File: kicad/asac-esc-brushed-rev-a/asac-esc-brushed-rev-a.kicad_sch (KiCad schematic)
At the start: 21 parts, among them J1 M1, J14 Conn_01x03, J2 Battery, J3 FC Connector, Q1 AO3480C, U1 HT7533S, U2 INA180A4, U3 STM32C011F6Px

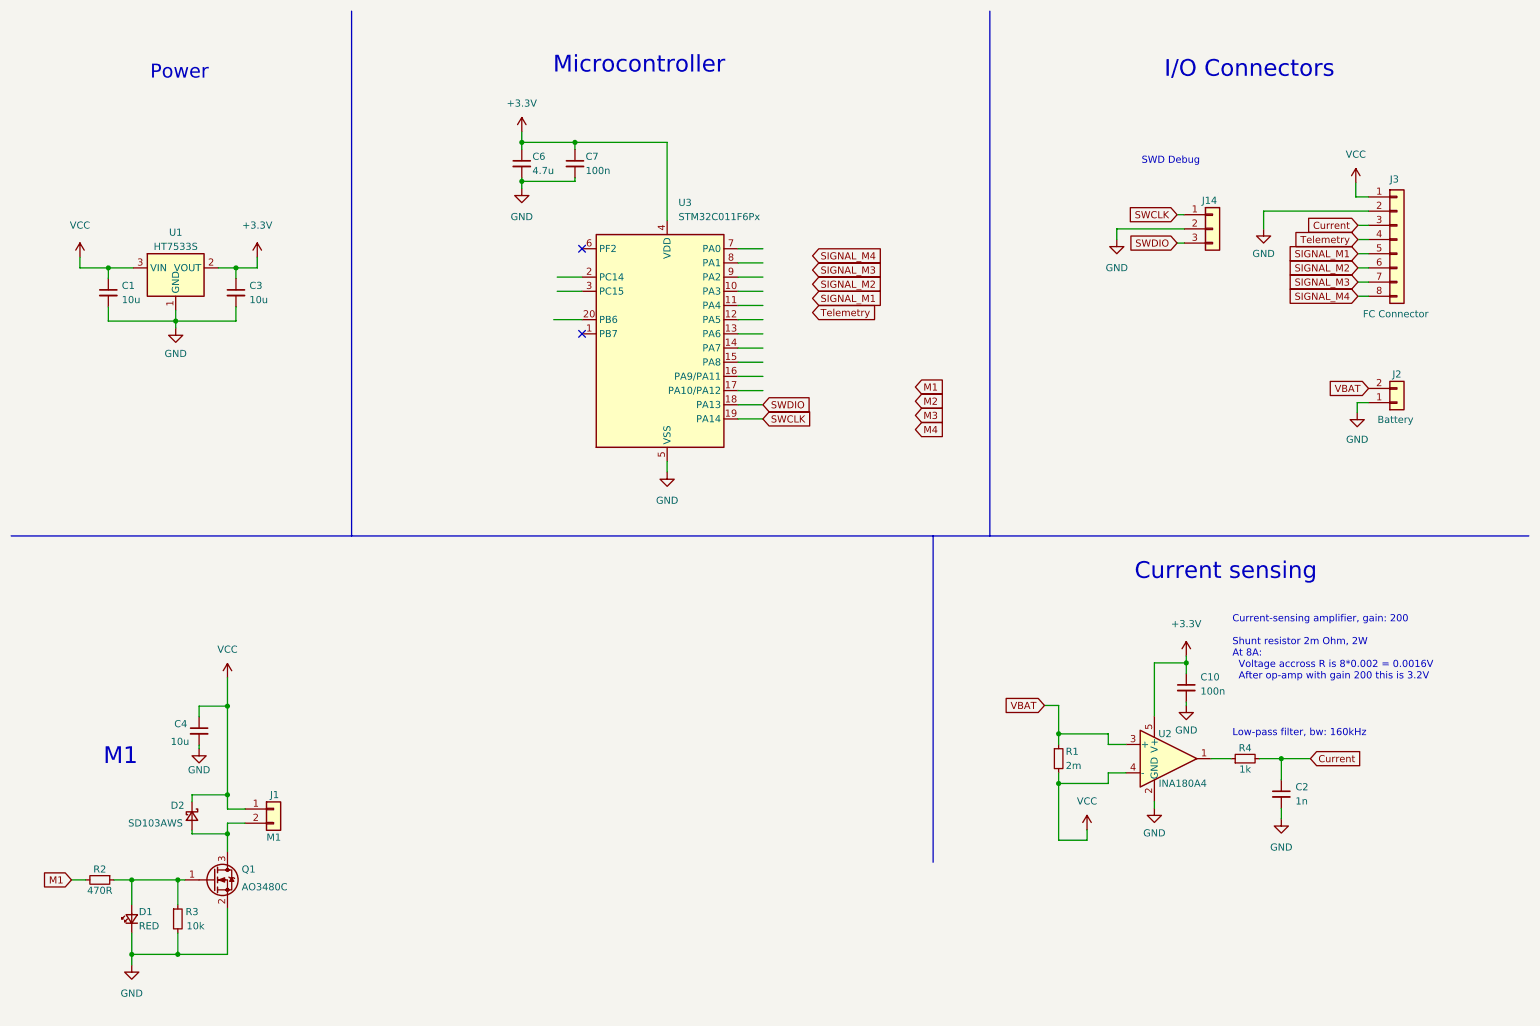
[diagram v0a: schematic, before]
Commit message: Finished rev A schematic, layout and routing
All that is left now is to add some graphics!
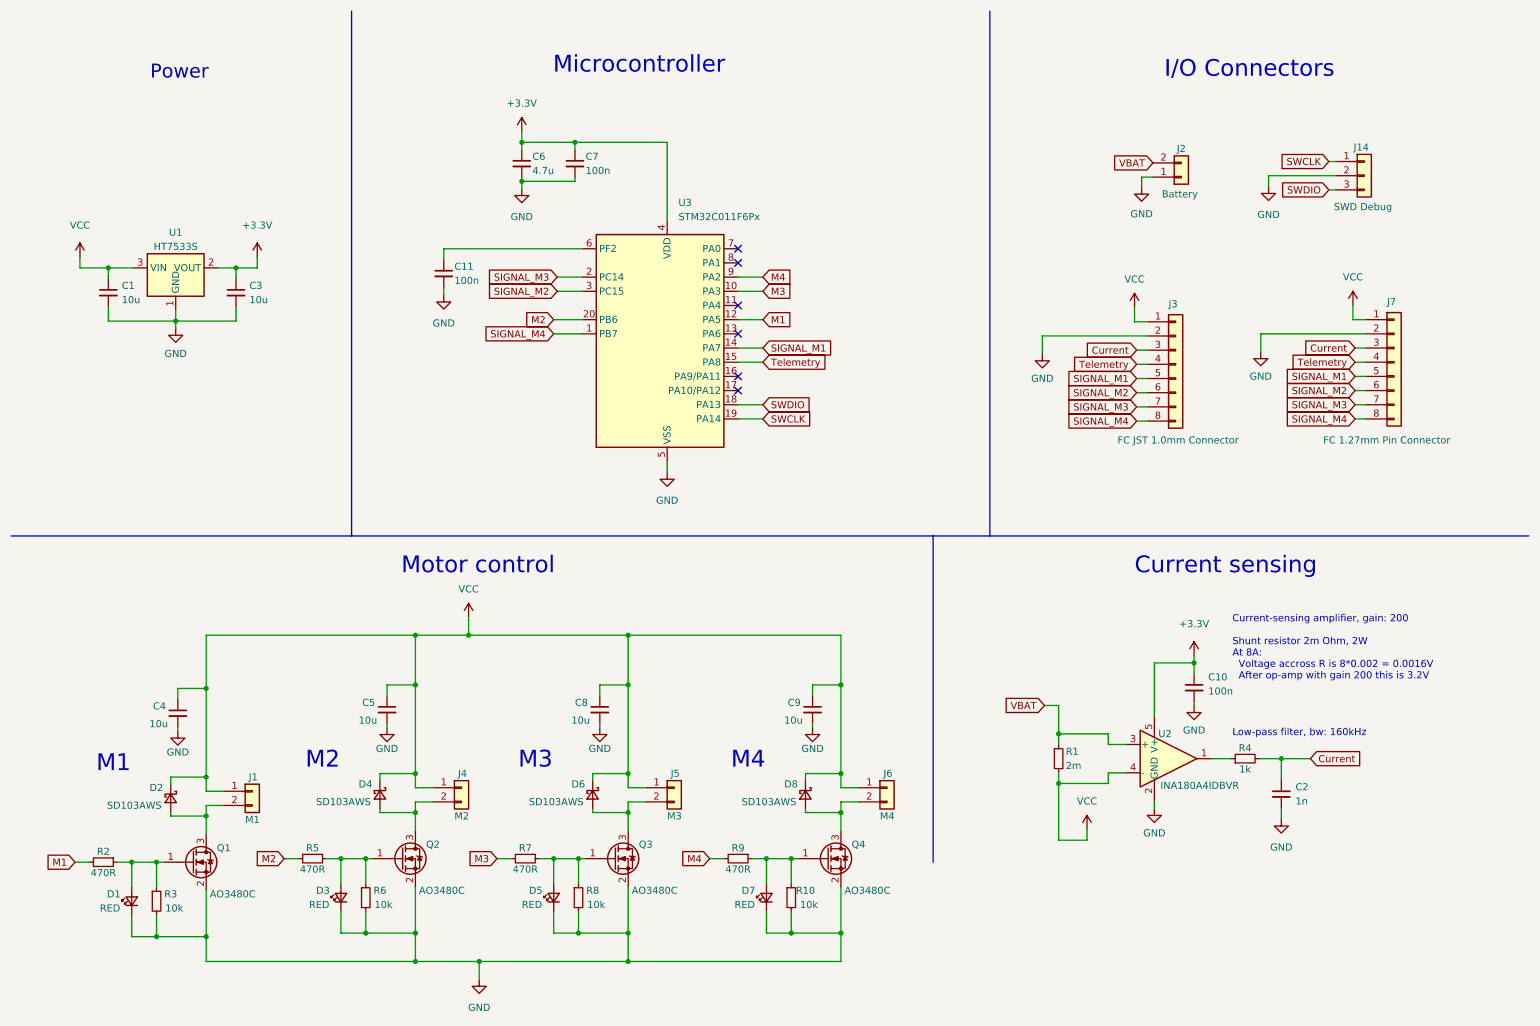
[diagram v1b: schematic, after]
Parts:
- added C11: 100n, Capacitor_SMD:C_0402_1005Metric, symbol Device:C_Small
- added C5, C8, C9: 10u, Capacitor_SMD:C_0805_2012Metric, symbol Device:C_Small
- added D3, D5, D7: RED, LED_SMD:LED_0603_1608Metric, symbol Device:LED_Small
- added D4, D6, D8: SD103AWS, Diode_SMD:D_SOD-323, symbol Device:D_Schottky_Small
- added J4: M2, Custom:Conn_01x02_VBAT_one_round, symbol Connector_Generic:Conn_01x02
- added J5: M3, Custom:Conn_01x02_VBAT_one_round, symbol Connector_Generic:Conn_01x02
- added J6: M4, Custom:Conn_01x02_VBAT_one_round, symbol Connector_Generic:Conn_01x02
- added J7: FC 1.27mm Pin Connector, Connector_PinHeader_1.27mm:PinHeader_1x08_P1.27mm_Vertical, symbol Connector_Generic:Conn_01x08
- added Q2, Q3, Q4: AO3480C, Package_TO_SOT_SMD:SOT-23, symbol Device:Q_NMOS_GSD
- added R10, R6, R8: 10k, Resistor_SMD:R_0402_1005Metric, symbol Device:R_Small
- added R5, R7, R9: 470R, Resistor_SMD:R_0402_1005Metric, symbol Device:R_Small
- J14: value Conn_01x03 -> SWD Debug
- J3: value FC Connector -> FC JST 1.0mm Connector
- U2: value INA180A4 -> INA180A4IDBVR
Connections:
- net Current: now also J7.3 (Pin_3)
- net GND: now also C11.2, C5.2, C8.2, C9.2, D3.1 (K), D5.1 (K), D7.1 (K), J7.2 (Pin_2), Q2.2 (S), Q3.2 (S), Q4.2 (S), R10.2, R6.2, R8.2
- net M1: now also U3.12 (PA5)
- net M2: now also U3.20 (PB6), R5.2
- net M3: now also U3.10 (PA3), R7.2
- net M4: now also U3.9 (PA2), R9.2
- net SIGNAL_M1: now also U3.14 (PA7), J7.5 (Pin_5)
- net SIGNAL_M2: now also U3.3 (PC15), J7.6 (Pin_6)
- net SIGNAL_M3: now also U3.2 (PC14), J7.7 (Pin_7)
- net SIGNAL_M4: now also U3.1 (PB7), J7.8 (Pin_8)
- net Telemetry: now also U3.15 (PA8), J7.4 (Pin_4)
- net VCC: now also C5.1, C8.1, C9.1, D4.1 (K), D6.1 (K), D8.1 (K), J4.1 (Pin_1), J5.1 (Pin_1), J6.1 (Pin_1), J7.1 (Pin_1)
- net at U3.6 (PF2): now also C11.1
- new net: D5.2 (A), Q3.1 (G), R7.1, R8.1
- new net: D4.2 (A), J4.2 (Pin_2), Q2.3 (D)
- new net: D6.2 (A), J5.2 (Pin_2), Q3.3 (D)
- new net: D7.2 (A), Q4.1 (G), R10.1, R9.1
- new net: D8.2 (A), J6.2 (Pin_2), Q4.3 (D)
- new net: D3.2 (A), Q2.1 (G), R5.1, R6.1
- no-connect marks 2 -> 6
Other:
- note added: "M2"
- note added: "M3"
- note added: "M4"
- note added: "Motor control"
- note removed: "SWD Debug"
- company: (none) -> Victor Krook
- title: (none) -> ASAC Brushed ESC
- moved on the sheet: C10, C4, D1, D2, J1, J14, J2, J3, Q1, R2, R3

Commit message: Rev. A ready for order!
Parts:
- D2: MPN (none) -> C2828423
- J14: footprint Custom:PinSocket_1x03_P2.54mm_Vertical_No_silk -> Connector_PinHeader_1.27mm:PinHeader_1x03_P1.27mm_Vertical
- Q1, U2: MPN (none) -> C188337
- U1: MPN (none) -> C347215
- U3: MPN (none) -> C5456198
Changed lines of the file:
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@@
+      (effects (font (size 1.27 1.27)) hide)
+    )
+    (property "MPN" "C2828423" (id 4) (at 41.275 153.67 90)
       (effects (font (size 1.27 1.27)) hide)
     )
@@
     )
     (property "Datasheet" "https://datasheet.lcsc.com/lcsc/2007301505_Alpha---Omega-Semicon-AO3480C_C705501.pdf" (id 3) (at 45.085 165.1 0)
+      (effects (font (size 1.27 1.27)) hide)
+    )
+    (property "MPN" "C188337" (id 4) (at 45.085 165.1 0)
       (effects (font (size 1.27 1.27)) hide)
     )
@@
     )
     (property "Datasheet" "https://www.st.com/resource/en/datasheet/stm32c011f6.pdf" (id 3) (at 127.635 73.025 0)
+      (effects (font (size 1.27 1.27)) hide)
+    )
+    (property "MPN" "C5456198" (id 4) (at 127.635 73.025 0)
       (effects (font (size 1.27 1.27)) hide)
     )
@@
       (effects (font (size 1.27 1.27)) (justify left))
     )
-    (property "Footprint" "Custom:PinSocket_1x03_P2.54mm_Vertical_No_silk" (id 2) (at 255.016 42.164 0)
+    (property "Footprint" "Connector_PinHeader_1.27mm:PinHeader_1x03_P1.27mm_Vertical" (id 2) (at 255.016 42.164 0)
       (effects (font (size 1.27 1.27)) hide)
     )
@@
       (effects (font (size 1.27 1.27)) hide)
     )
+    (property "MPN" "C188337" (id 4) (at 219.964 146.558 0)
+      (effects (font (size 1.27 1.27)) hide)
+    )
     (pin "1")
     (pin "2")
@@
       (effects (font (size 1.27 1.27)) hide)
     )
+    (property "MPN" "C347215" (id 4) (at 42.164 61.214 0)
+      (effects (font (size 1.27 1.27)) hide)
+    )
     (pin "1")
     (pin "2")
@@
     )
     (path "/414430b5-43c2-4577-8f0e-dfbfd11a4f1a"
-      (reference "J14") (unit 1) (value "SWD Debug") (footprint "Custom:PinSocket_1x03_P2.54mm_Vertical_No_silk")
+      (reference "J14") (unit 1) (value "SWD Debug") (footprint "Connector_PinHeader_1.27mm:PinHeader_1x03_P1.27mm_Vertical")
     )
     (path "/2e073498-4b53-441f-84e8-fbb53c826168"
